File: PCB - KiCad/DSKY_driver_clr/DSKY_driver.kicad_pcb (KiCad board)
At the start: 2 copper layers, 43 x 92.3 mm, 229 parts, among them IC3 ATSAMD21E, J1 FX6-60S, J2 FX6-60S, J3 FX6-60S, J4 CUI_power_jack, Q2 reset, U1 HV507, U2 LT3468, U3 AP2204K-3.3, U4 AP2204K-5.0, U5 HV507, U6 LT3468, U7 HV507, U8 CD40109B, X1 USB_micro

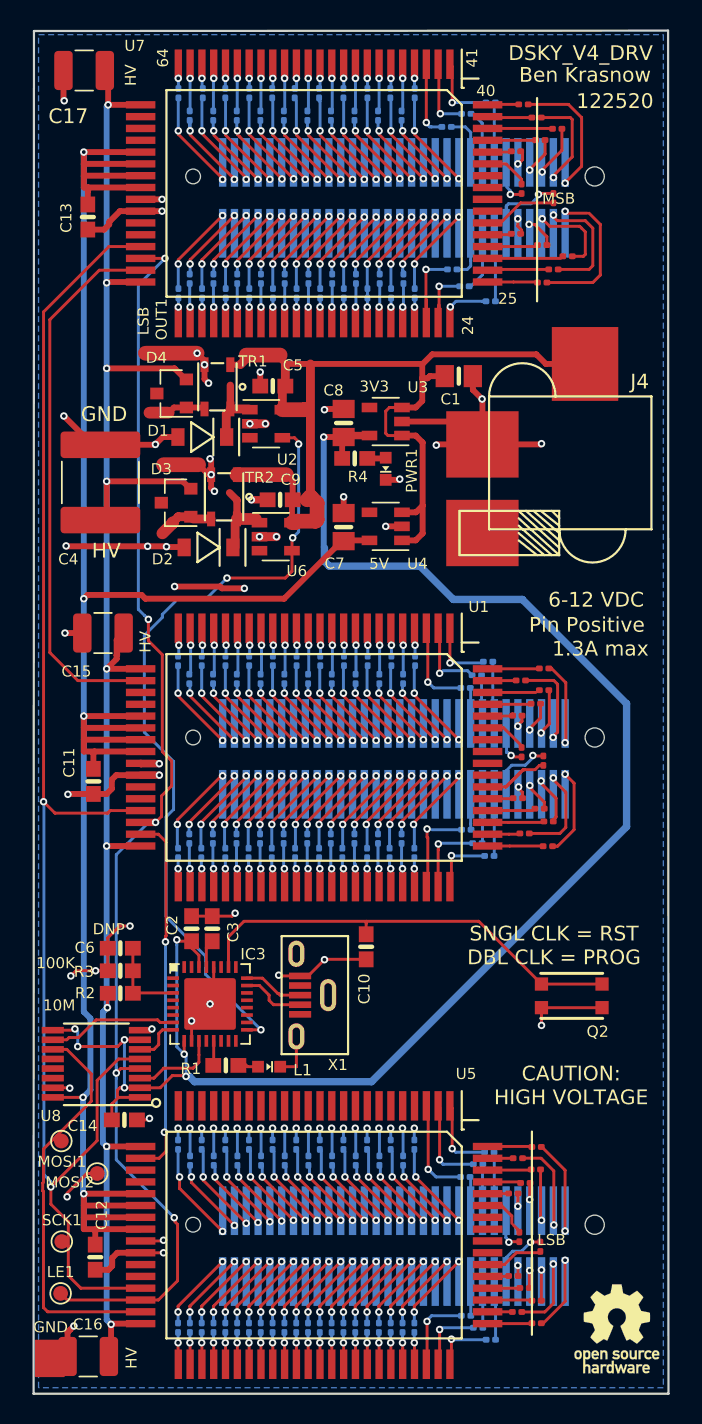
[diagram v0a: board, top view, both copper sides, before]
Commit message: Fine tuning resistor placement
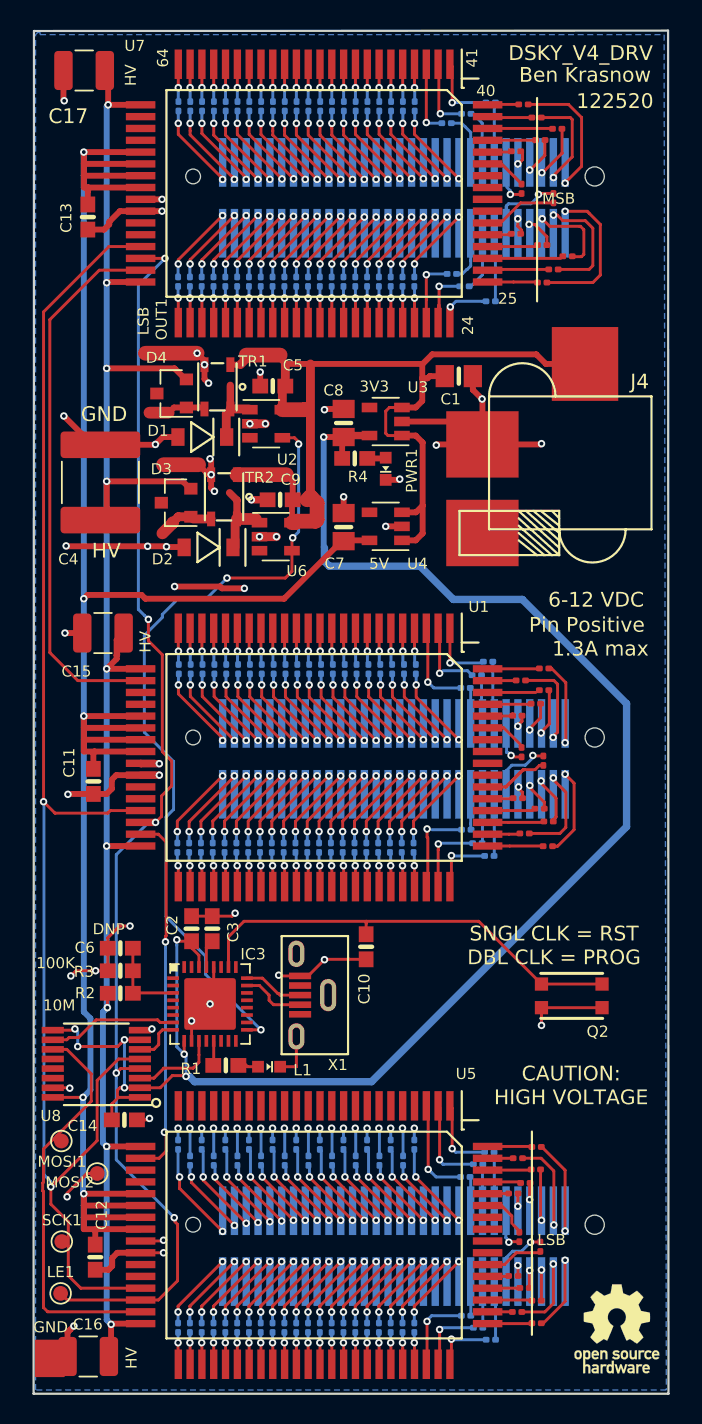
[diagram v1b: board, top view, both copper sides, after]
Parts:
- C10: value 10n -> 10nF
- C15, C16, C17: value .22u -> .22uF
- C5, C9: value 6.3uF -> 6.8uF
- C7, C8: value 2.2u -> 2.2uF
- J4: value CUI_power_jack -> PJ-006B-SMT
- R10, R100, R101, R102, R103, R104, R105, R106, R107, R108, R109, R11, R110, R111, R112, R113, R114, R115, R116, R117, R118, R119, R12, R120, R121, R122, R123, R124, R125, R126, R127, R128, R129, R13, R130, R131, R132, R133, R134, R135, R136, R137, R138, R139, R14, R140, R141, R142, R143, R144, R145, R146, R147, R148, R149, R15, R150, R151, R152, R153, R154, R155, R156, R157, R158, R159, R16, R160, R161, R162, R163, R164, R165, R166, R167, R168, R169, R17, R170, R171, R172, R173, R174, R175, R176, R177, R178, R179, R18, R180, R181, R182, R183, R184, R19, R20, R21, R22, R23, R24, R25, R26, R27, R28, R29, R30, R31, R32, R33, R34, R35, R36, R37, R38, R39, R40, R41, R42, R43, R44, R45, R46, R47, R48, R49, R5, R50, R51, R52, R53, R54, R55, R56, R57, R58, R59, R6, R60, R61, R62, R63, R64, R65, R66, R67, R68, R69, R7, R70, R71, R72, R73, R74, R75, R76, R77, R78, R79, R8, R80, R81, R82, R83, R84, R85, R86, R87, R88, R89, R9, R90, R91, R92, R93, R94, R95, R96, R97, R98, R99: value 100K -> 75K
- X1: value USB_micro -> Molex 105133
- moved R153 0.90 mm to (146.8, 42.8)
- moved R56 0.89 mm to (148.4, 42.8)
- moved R151 0.89 mm to (145.2, 42.8)
- moved R159 0.89 mm to (140.4, 42.8)
- moved R62 0.89 mm to (153.2, 42.8)
- moved R61 0.89 mm to (150.0, 42.8)
- moved R67 0.89 mm to (142.0, 42.8)
- moved R152 0.89 mm to (151.6, 42.8)
- moved R155 0.89 mm to (143.6, 42.8)
- moved R158 0.89 mm to (138.8, 42.8)
- moved R54 0.89 mm to (154.8, 42.8)
- moved R10 0.79 mm to (142.0, 54.7)
- moved R11 0.79 mm to (150.0, 54.7)
- moved R14 0.79 mm to (140.4, 54.7)
- moved R15 0.79 mm to (148.4, 54.7)
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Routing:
- net Net-(R92-Pad1): track 6.26 -> 0.00 mm, vias 1 -> 0
- net Net-(J2-Pad50): track 0.00 -> 5.90 mm, vias 1 -> 2
- net Net-(J2-Pad51): track 0.00 -> 5.85 mm, vias 1 -> 2
- net Net-(J2-Pad48): track 0.00 -> 5.84 mm, vias 1 -> 2
- net Net-(R38-Pad1): track 6.40 -> 0.80 mm, vias 1 -> 0
- net Net-(R28-Pad1): track 6.34 -> 0.77 mm, vias 1 -> 0
- net Net-(R36-Pad1): track 6.25 -> 0.75 mm, vias 1 -> 0
- net Net-(R82-Pad1): track 6.22 -> 0.73 mm
- net Net-(R27-Pad1): track 6.22 -> 0.77 mm, vias 1 -> 0
- net Net-(R70-Pad1): track 6.22 -> 0.80 mm, vias 1 -> 0
- net Net-(R40-Pad1): track 6.15 -> 0.80 mm, vias 1 -> 0
- net Net-(R72-Pad1): track 6.17 -> 0.82 mm, vias 1 -> 0
- net Net-(R52-Pad1): track 6.17 -> 0.85 mm, vias 1 -> 0
- net Net-(R88-Pad1): track 5.30 -> 0.00 mm, vias 1 -> 0
- net Net-(J2-Pad45): track 0.00 -> 5.26 mm, vias 1 -> 2
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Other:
- net class Default: clearance 0.2 -> 0.1778
- rule trace_clearance: 0.2 -> 0.1778
- board text added: "see notes"

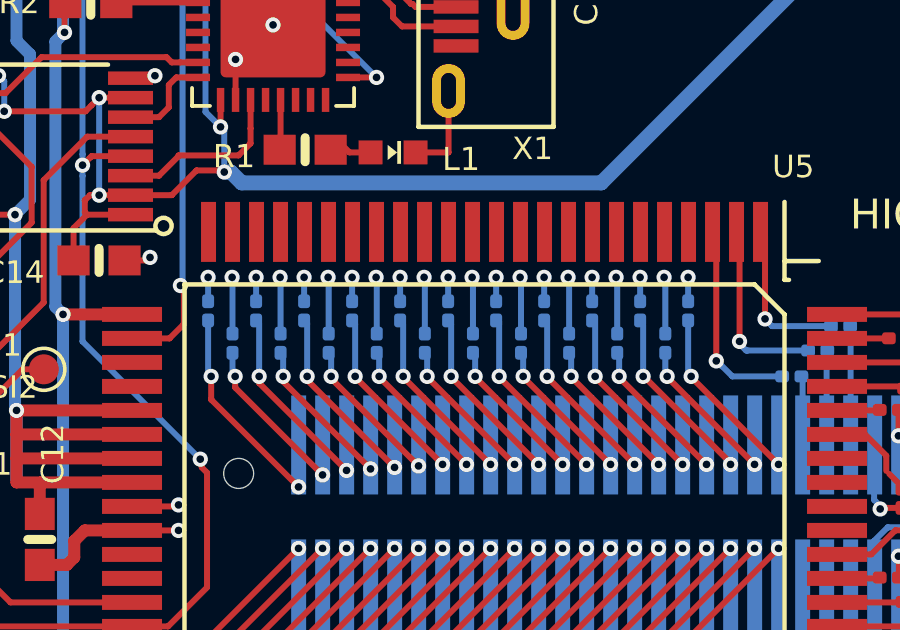
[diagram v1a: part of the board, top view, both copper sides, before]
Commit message: more reorganization of resistor layout
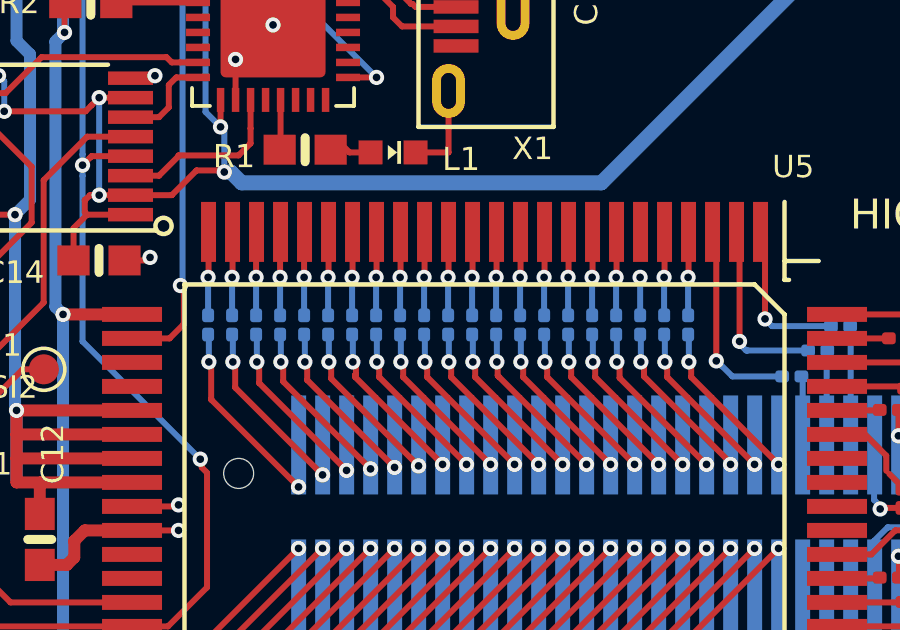
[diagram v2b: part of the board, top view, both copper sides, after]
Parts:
- moved R129 0.61 mm to (154.0, 113.6)
- moved R124 0.61 mm to (152.4, 113.6)
- moved R120 0.61 mm to (150.8, 113.6)
- moved R117 0.61 mm to (149.2, 113.6)
- moved R118 0.61 mm to (147.6, 113.6)
- moved R121 0.61 mm to (146.0, 113.6)
- moved R132 0.61 mm to (144.4, 113.6)
- moved R123 0.61 mm to (142.8, 113.6)
- moved R99 0.61 mm to (141.2, 113.6)
- moved R97 0.61 mm to (139.6, 113.6)
- moved R100 0.47 mm to (138.8, 113.6)
- moved R119 0.47 mm to (142.0, 113.6)
- moved R122 0.47 mm to (145.2, 113.6)
- moved R125 0.47 mm to (146.8, 113.6)
- moved R127 0.47 mm to (143.6, 113.6)
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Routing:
- net Net-(U5-Pad15): track 0.00 -> 2.85 mm, vias 0 -> 1
- net Net-(U5-Pad20): track 0.00 -> 2.82 mm, vias 0 -> 1
- net Net-(U5-Pad18): track 0.00 -> 2.80 mm, vias 0 -> 1
- net Net-(U5-Pad13): track 0.00 -> 2.80 mm, vias 0 -> 1
- net Net-(U5-Pad12): track 0.00 -> 2.77 mm, vias 0 -> 1
- net Net-(U5-Pad17): track 0.00 -> 2.77 mm, vias 0 -> 1
- net Net-(U5-Pad16): track 0.00 -> 2.77 mm, vias 0 -> 1
- net Net-(U5-Pad5): track 0.00 -> 2.77 mm, vias 0 -> 1
- net Net-(U5-Pad21): track 0.00 -> 2.77 mm, vias 0 -> 1
- net Net-(U5-Pad14): track 0.00 -> 2.75 mm, vias 0 -> 1
- net Net-(U5-Pad19): track 0.00 -> 2.75 mm, vias 0 -> 1
- net Net-(U5-Pad23): track 0.00 -> 2.74 mm, vias 0 -> 1
- net Net-(U5-Pad9): track 0.00 -> 2.74 mm, vias 0 -> 1
- net Net-(U5-Pad10): track 0.00 -> 2.72 mm, vias 0 -> 1
- net Net-(U5-Pad7): track 0.00 -> 2.72 mm, vias 0 -> 1
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
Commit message: Latest draft PCB update
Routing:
- net Net-(R12-Pad1): track 0.00 -> 6.01 mm
- net Net-(J1-Pad58): track 5.68 -> 0.00 mm
- net Net-(R173-Pad2): track 0.00 -> 2.69 mm
- net Net-(J3-Pad4): track 1.12 -> 0.00 mm
- net Net-(R65-Pad1): track 2.12 -> 2.78 mm
- net Net-(R96-Pad2): track 2.12 -> 2.71 mm
- net Net-(R90-Pad1): track 1.90 -> 2.46 mm
- net Net-(R180-Pad2): track 1.97 -> 2.48 mm
- net Net-(R44-Pad1): track 3.09 -> 3.60 mm
- net Net-(R177-Pad2): track 1.08 -> 1.59 mm
